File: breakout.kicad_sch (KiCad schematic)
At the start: 7 parts, among them J1 Conn_01x03, J2 Conn_01x02

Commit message: v1.0
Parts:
- added J3: Conn_01x02, Connector_PinHeader_2.54mm:PinHeader_1x02_P2.54mm_Vertical, symbol Connector_Generic:Conn_01x02
- J2: footprint TerminalBlock_Phoenix:TerminalBlock_Phoenix_PTSM-0,5-2-HV-2.5-SMD_1x02-1MP_P2.50mm_Vertical -> DUST:PTSM 0.5-2-HH-2.5-SMD
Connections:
- net GND: now also J3.2 (Pin_2)
- net at C1.1, D1.2 (A), J2.1 (Pin_1)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: now also J3.1 (Pin_1)
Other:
- moved on the sheet: C2, D1, R2

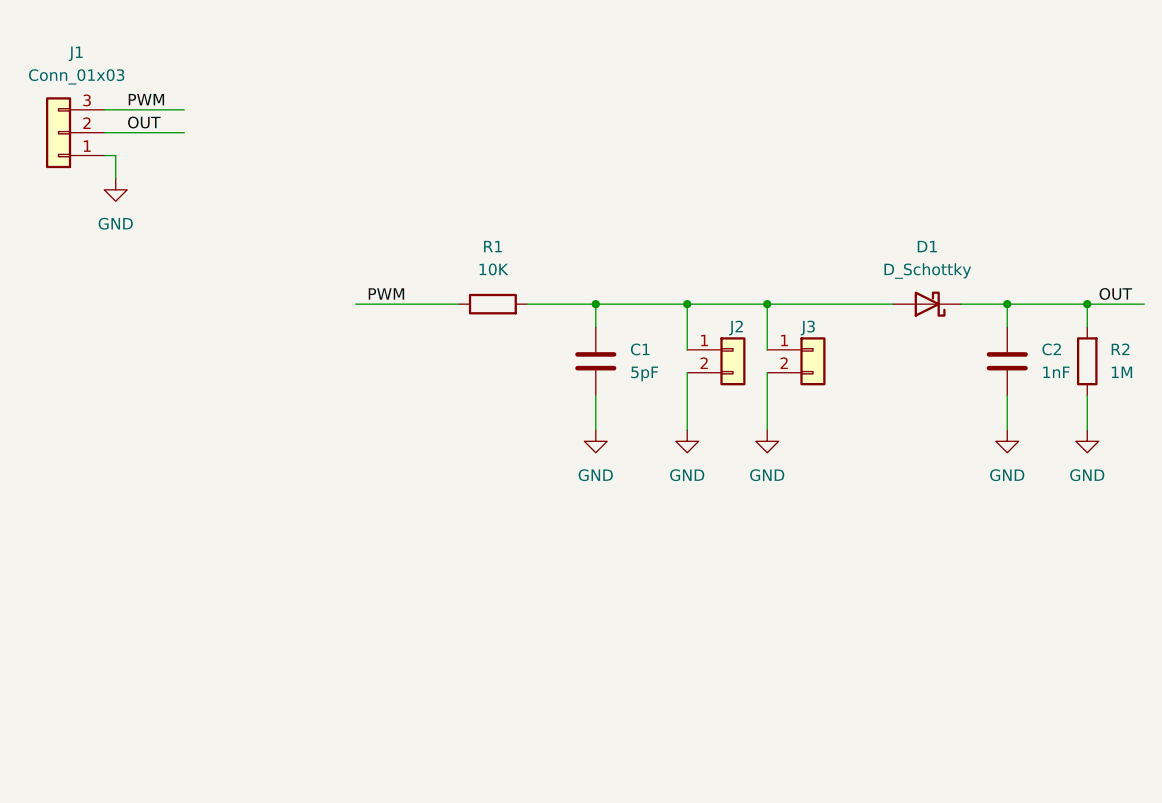
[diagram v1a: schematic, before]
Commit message: add discharge circuit
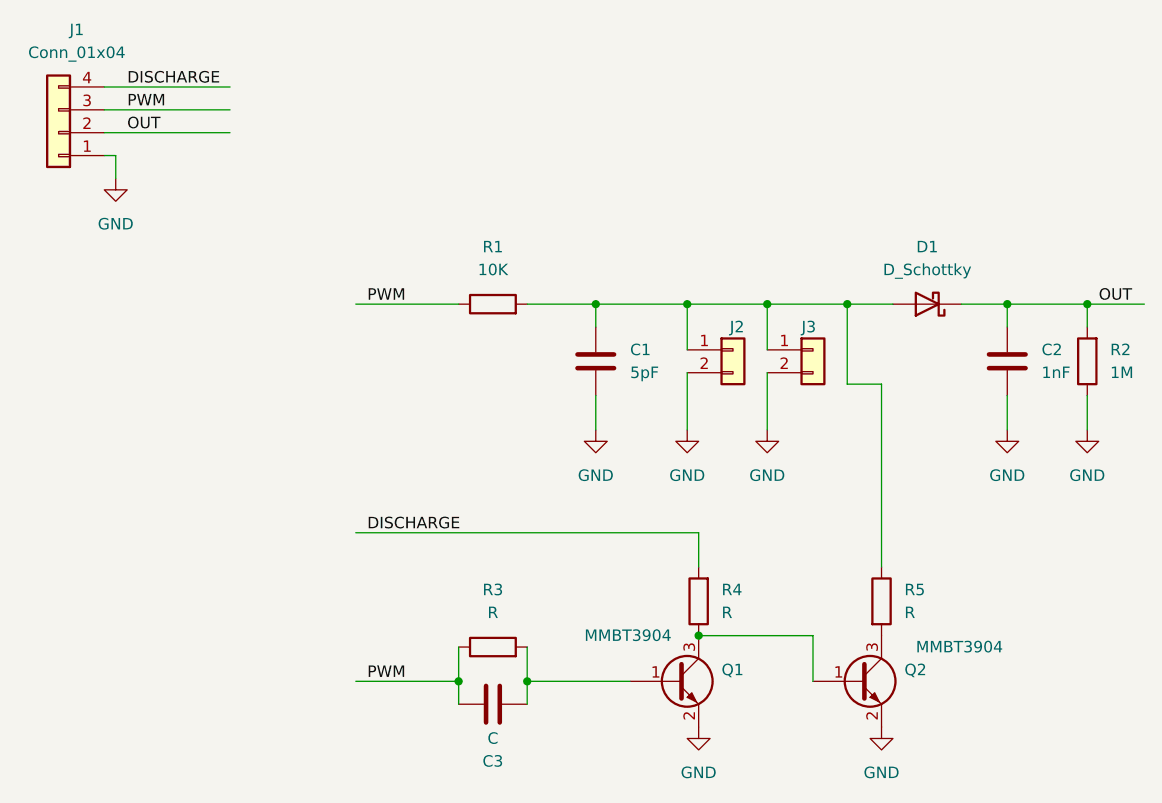
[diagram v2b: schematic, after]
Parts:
- removed J1: Conn_01x03, Connector_PinHeader_2.54mm:PinHeader_1x03_P2.54mm_Vertical, symbol Connector_Generic:Conn_01x03
- added C3: C, Capacitor_SMD:C_0603_1608Metric, symbol Device:C
- added J1: Conn_01x04, Connector_PinHeader_2.54mm:PinHeader_1x04_P2.54mm_Vertical, symbol Connector_Generic:Conn_01x04
- added Q1, Q2: MMBT3904, Package_TO_SOT_SMD:SOT-23, symbol Transistor_BJT:MMBT3904
- added R3, R4, R5: R, Resistor_SMD:R_0603_1608Metric, symbol Device:R
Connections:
- net GND: now also J1.1 (Pin_1), Q1.2 (E), Q2.2 (E)
- net OUT: now also J1.2 (Pin_2)
- net PWM: now also C3.2, J1.3 (Pin_3), R3.1
- net at C1.1, D1.2 (A), J2.1 (Pin_1)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: now also R5.1
- new net: Q1.3 (C), Q2.1 (B), R4.1
- new net: C3.1, Q1.1 (B), R3.2
- new net: Q2.3 (C), R5.2
- new net DISCHARGE: J1.4 (Pin_4), R4.2
